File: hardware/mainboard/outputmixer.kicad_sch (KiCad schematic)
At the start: 15 parts, among them J1 EXT, J117 MIX, U12 TL074, U6 TL074

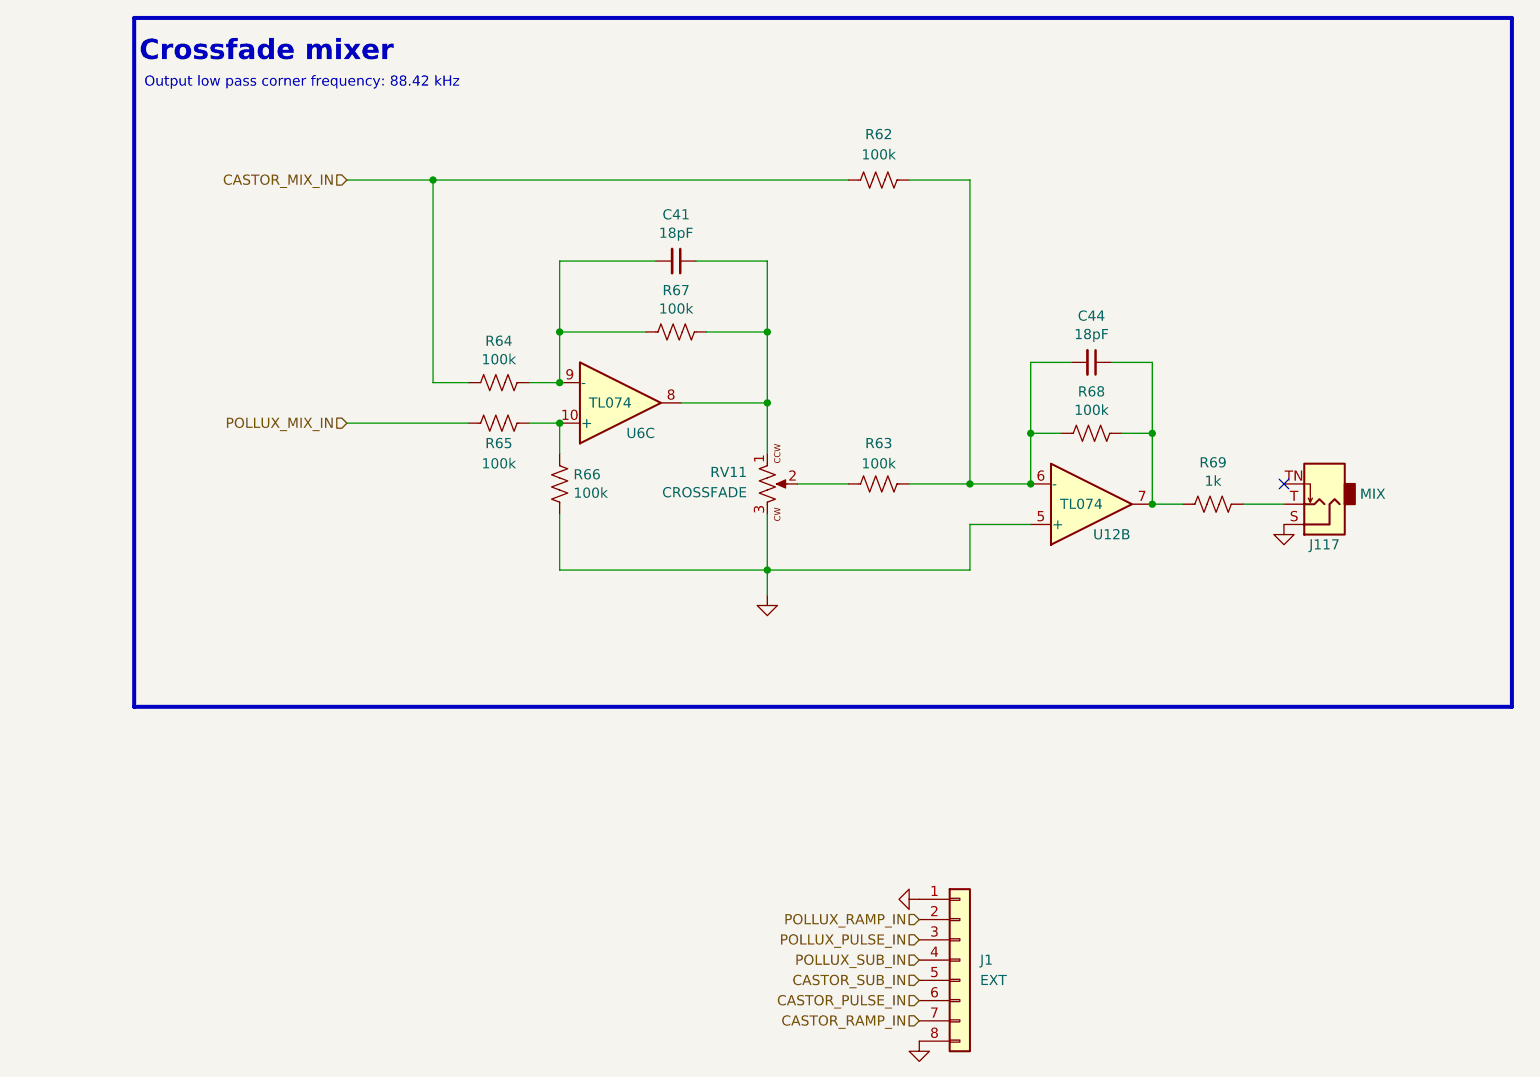
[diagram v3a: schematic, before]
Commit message: Reannotate schematic
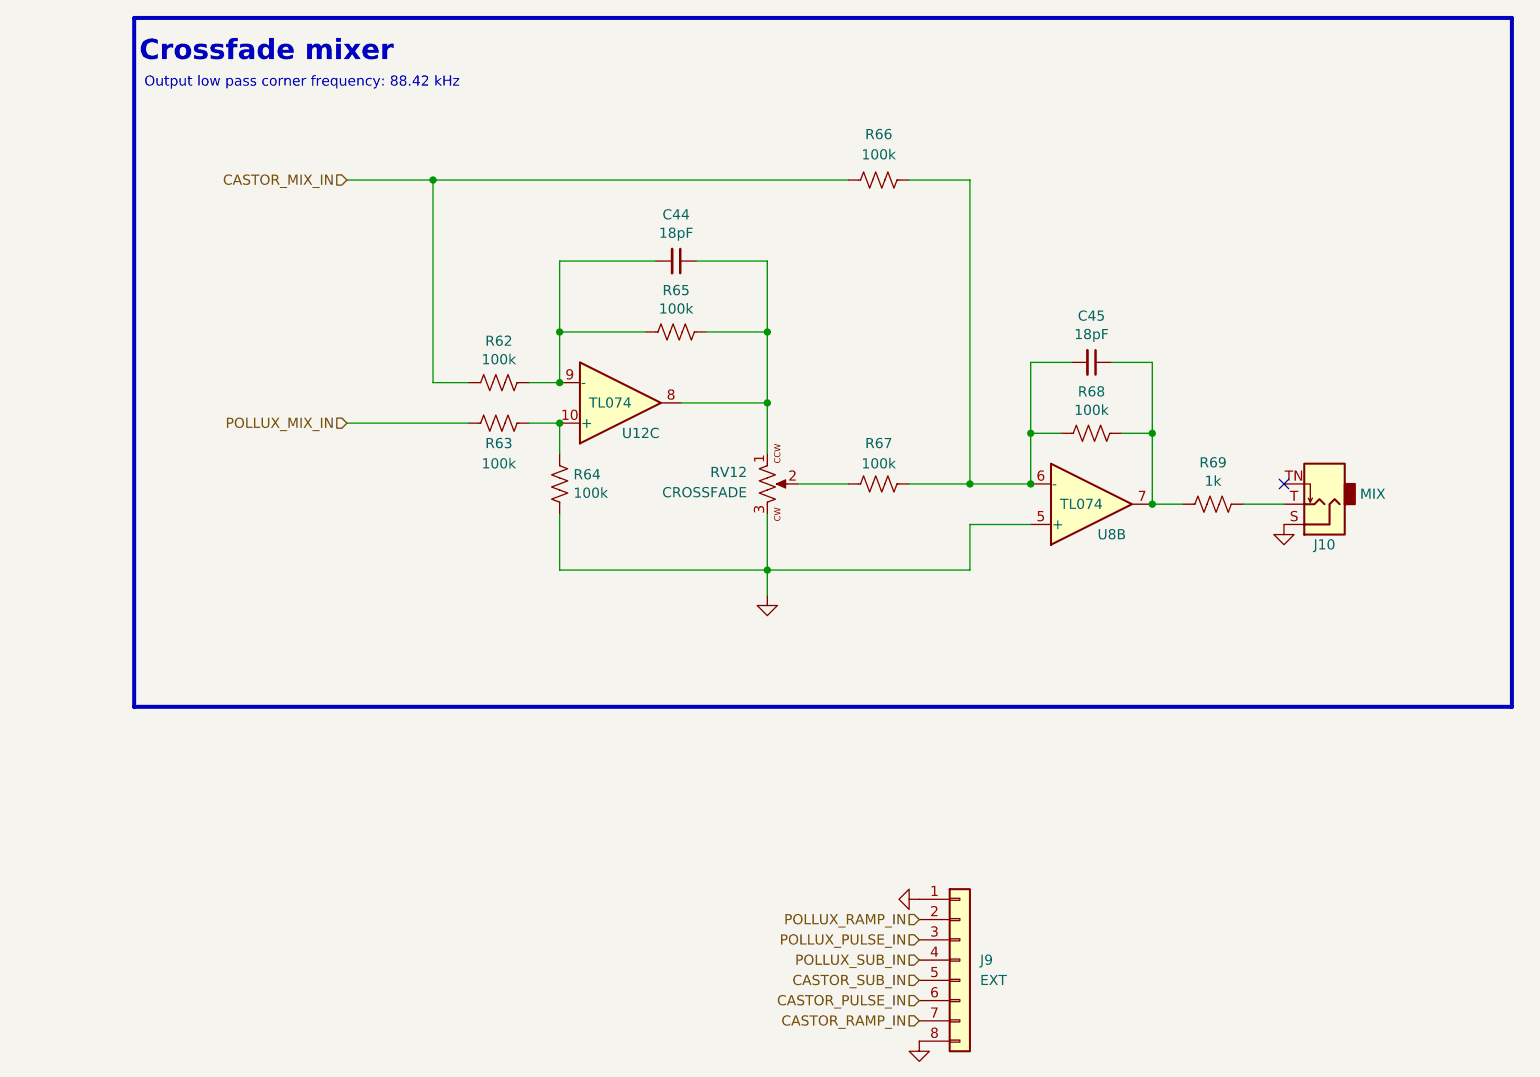
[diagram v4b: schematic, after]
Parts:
- renumbered C41 to C44, C44 to C45, J117 to J10, J1 to J9, R64 to R62, R65 to R63, R66 to R64, R67 to R65, R62 to R66, R63 to R67, RV11 to RV12, U6 to U12, U12 to U8
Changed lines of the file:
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@@
   (symbol (lib_id "Device:R_US") (at 99.695 69.85 270) (unit 1)
     (in_bom yes) (on_board yes)
-    (property "Reference" "R64" (id 0) (at 99.695 64.643 90))
+    (property "Reference" "R62" (id 0) (at 99.695 64.643 90))
     (property "Value" "100k" (id 1) (at 99.695 66.9544 90))
     (property "Footprint" "Resistor_SMD:R_0402_1005Metric_Pad0.72x0.64mm_HandSolder" (id 2) (at 99.441 70.866 90)
@@
   (symbol (lib_id "Device:R_US") (at 99.695 74.93 270) (unit 1)
     (in_bom yes) (on_board yes)
-    (property "Reference" "R65" (id 0) (at 99.695 77.47 90))
+    (property "Reference" "R63" (id 0) (at 99.695 77.47 90))
     (property "Value" "100k" (id 1) (at 99.695 80.01 90))
     (property "Footprint" "Resistor_SMD:R_0402_1005Metric_Pad0.72x0.64mm_HandSolder" (id 2) (at 99.441 75.946 90)
@@
   (symbol (lib_id "Device:R_US") (at 107.315 82.55 180) (unit 1)
     (in_bom yes) (on_board yes)
-    (property "Reference" "R66" (id 0) (at 109.0422 81.3816 0)
+    (property "Reference" "R64" (id 0) (at 109.0422 81.3816 0)
       (effects (font (size 1.27 1.27)) (justify right))
     )
@@
   (symbol (lib_id "Device:R_US") (at 121.92 63.5 90) (unit 1)
     (in_bom yes) (on_board yes)
-    (property "Reference" "R67" (id 0) (at 121.92 58.293 90))
+    (property "Reference" "R65" (id 0) (at 121.92 58.293 90))
     (property "Value" "100k" (id 1) (at 121.92 60.6044 90))
     (property "Footprint" "Resistor_SMD:R_0402_1005Metric_Pad0.72x0.64mm_HandSolder" (id 2) (at 122.174 62.484 90)
@@
   (symbol (lib_id "Device:R_US") (at 147.32 44.45 90) (unit 1)
     (in_bom yes) (on_board yes)
-    (property "Reference" "R62" (id 0) (at 147.32 38.735 90))
+    (property "Reference" "R66" (id 0) (at 147.32 38.735 90))
     (property "Value" "100k" (id 1) (at 147.32 41.275 90))
     (property "Footprint" "Resistor_SMD:R_0402_1005Metric_Pad0.72x0.64mm_HandSolder" (id 2) (at 147.574 43.434 90)
@@
   (symbol (lib_id "Device:C_Small") (at 121.92 54.61 270) (unit 1)
     (in_bom yes) (on_board yes)
-    (property "Reference" "C41" (id 0) (at 121.92 48.7934 90))
+    (property "Reference" "C44" (id 0) (at 121.92 48.7934 90))
     (property "Value" "18pF" (id 1) (at 121.92 51.1048 90))
     (property "Footprint" "Capacitor_SMD:C_0402_1005Metric_Pad0.74x0.62mm_HandSolder" (id 2) (at 121.92 54.61 0)
@@
   (symbol (lib_id "Device:R_US") (at 147.32 82.55 90) (unit 1)
     (in_bom yes) (on_board yes)
-    (property "Reference" "R63" (id 0) (at 147.32 77.47 90))
+    (property "Reference" "R67" (id 0) (at 147.32 77.47 90))
     (property "Value" "100k" (id 1) (at 147.32 80.01 90))
     (property "Footprint" "Resistor_SMD:R_0402_1005Metric_Pad0.72x0.64mm_HandSolder" (id 2) (at 147.574 81.534 90)
@@
   (symbol (lib_id "power:GND") (at 133.35 96.52 0) (unit 1)
     (in_bom yes) (on_board yes)
-    (property "Reference" "#PWR0120" (id 0) (at 133.35 102.87 0)
+    (property "Reference" "#PWR090" (id 0) (at 133.35 102.87 0)
       (effects (font (size 1.27 1.27)) hide)
     )
@@
   (symbol (lib_id "Device:C_Small") (at 173.99 67.31 270) (unit 1)
     (in_bom yes) (on_board yes)
-    (property "Reference" "C44" (id 0) (at 173.99 61.4934 90))
+    (property "Reference" "C45" (id 0) (at 173.99 61.4934 90))
     (property "Value" "18pF" (id 1) (at 173.99 63.8048 90))
     (property "Footprint" "Capacitor_SMD:C_0402_1005Metric_Pad0.74x0.62mm_HandSolder" (id 2) (at 173.99 67.31 0)
@@
   (symbol (lib_id "Connector_Generic:Conn_01x08") (at 157.48 142.24 0) (unit 1)
     (in_bom yes) (on_board yes) (fields_autoplaced)
-    (property "Reference" "J1" (id 0) (at 160.02 142.2399 0)
+    (property "Reference" "J9" (id 0) (at 160.02 142.2399 0)
       (effects (font (size 1.27 1.27)) (justify left))
     )
@@
   (symbol (lib_id "power:GND") (at 152.4 152.4 0) (unit 1)
     (in_bom yes) (on_board yes) (fields_autoplaced)
-    (property "Reference" "#PWR0128" (id 0) (at 152.4 158.75 0)
+    (property "Reference" "#PWR092" (id 0) (at 152.4 158.75 0)
       (effects (font (size 1.27 1.27)) hide)
     )
@@
   (symbol (lib_id "winterbloom:TL074") (at 173.99 85.09 0) (mirror x) (unit 2)
     (in_bom yes) (on_board yes)
-    (property "Reference" "U12" (id 0) (at 176.53 88.9 0))
+    (property "Reference" "U8" (id 0) (at 176.53 88.9 0))
     (property "Value" "TL074" (id 1) (at 172.72 85.09 0))
     (property "Footprint" "Package_SO:TSSOP-14_4.4x5mm_P0.65mm" (id 2) (at 173.99 95.25 0)
@@
   (symbol (lib_id "winterbloom:Eurorack_Mono_Jack") (at 203.2 83.82 0) (unit 1)
     (in_bom yes) (on_board yes)
-    (property "Reference" "J117" (id 0) (at 203.2 90.17 0))
+    (property "Reference" "J10" (id 0) (at 203.2 90.17 0))
     (property "Value" "MIX" (id 1) (at 207.645 83.82 0)
       (effects (font (size 1.27 1.27)) (justify left))
@@
   (symbol (lib_id "winterbloom:Eurorack_Pot") (at 133.35 82.55 90) (mirror x) (unit 1)
     (in_bom yes) (on_board yes) (fields_autoplaced)
-    (property "Reference" "RV11" (id 0) (at 130.81 81.0894 90)
+    (property "Reference" "RV12" (id 0) (at 130.81 81.0894 90)
       (effects (font (size 1.27 1.27)) (justify left))
     )
@@
   (symbol (lib_id "winterbloom:TL074") (at 114.935 72.39 0) (mirror x) (unit 3)
     (in_bom yes) (on_board yes)
-    (property "Reference" "U6" (id 0) (at 117.475 76.2 0))
+    (property "Reference" "U12" (id 0) (at 117.475 76.2 0))
     (property "Value" "TL074" (id 1) (at 113.665 72.39 0))
     (property "Footprint" "Package_SO:TSSOP-14_4.4x5mm_P0.65mm" (id 2) (at 114.935 82.55 0)
@@
   (symbol (lib_id "power:GND") (at 152.4 134.62 270) (unit 1)
     (in_bom yes) (on_board yes) (fields_autoplaced)
-    (property "Reference" "#PWR0129" (id 0) (at 146.05 134.62 0)
+    (property "Reference" "#PWR091" (id 0) (at 146.05 134.62 0)
       (effects (font (size 1.27 1.27)) hide)
     )
@@
   (symbol (lib_id "power:GND") (at 198.12 87.63 0) (unit 1)
     (in_bom yes) (on_board yes)
-    (property "Reference" "#PWR0155" (id 0) (at 198.12 93.98 0)
-      (effects (font (size 1.27 1.27)) hide)
-    )
+    (property "Reference" "#PWR093" (id 0) (at 198.12 93.98 0)
+      (effects (font (size 1.27 1.27)) hide)
+    )

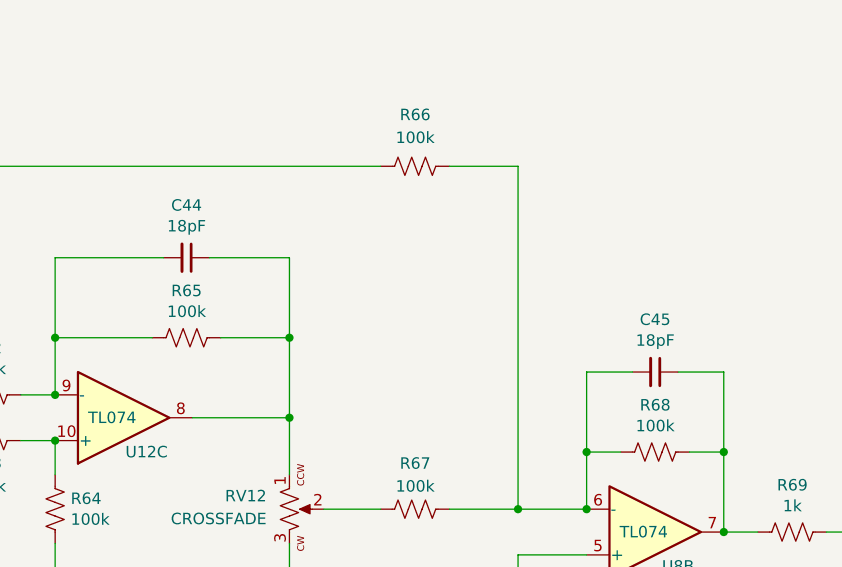
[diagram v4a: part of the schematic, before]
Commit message: Normalize component values
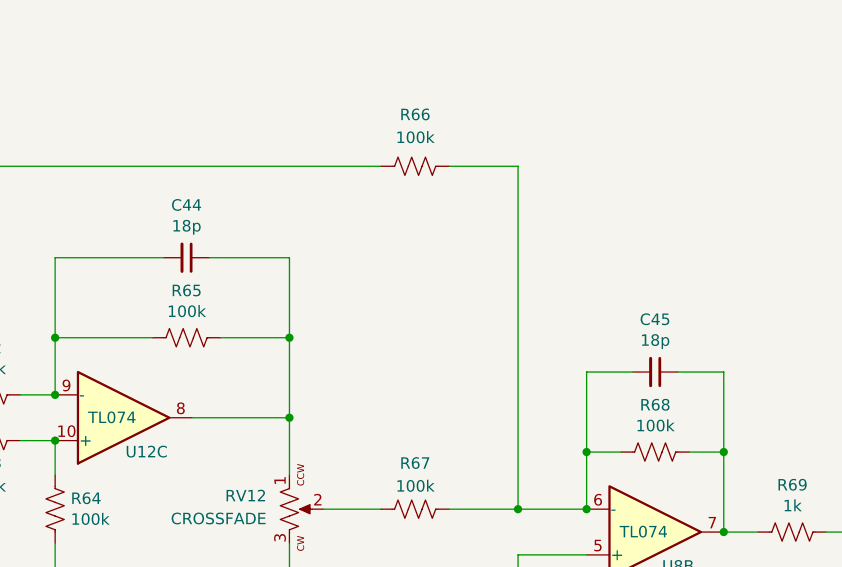
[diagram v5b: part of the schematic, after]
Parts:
- C44, C45: value 18pF -> 18p
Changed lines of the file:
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@@
     (in_bom yes) (on_board yes)
     (property "Reference" "C44" (id 0) (at 121.92 48.7934 90))
-    (property "Value" "18pF" (id 1) (at 121.92 51.1048 90))
+    (property "Value" "18p" (id 1) (at 121.92 51.1048 90))
     (property "Footprint" "Capacitor_SMD:C_0402_1005Metric_Pad0.74x0.62mm_HandSolder" (id 2) (at 121.92 54.61 0)
       (effects (font (size 1.27 1.27)) hide)
@@
     (in_bom yes) (on_board yes)
     (property "Reference" "C45" (id 0) (at 173.99 61.4934 90))
-    (property "Value" "18pF" (id 1) (at 173.99 63.8048 90))
+    (property "Value" "18p" (id 1) (at 173.99 63.8048 90))
     (property "Footprint" "Capacitor_SMD:C_0402_1005Metric_Pad0.74x0.62mm_HandSolder" (id 2) (at 173.99 67.31 0)
       (effects (font (size 1.27 1.27)) hide)

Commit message: Switch audio filter caps to 0603. Start auditing BOM
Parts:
- C44, C45: Reqs audio filter, 16v+ -> Eurorack level audio filter, 16 V; finalized yes -> (none); mpn MF-CAP-0603-18pF -> (none); mpn alt GCM1885C2A180JA16D -> (none); mpn specs 5% 50v -> (none)
- J10: finalized (none) -> yes
- R62, R63, R64, R65, R66, R67, R68: Reqs 1%, 2mW, audio path -> Eurorack level audio, 1%, 2 mW; finalized yes -> (none); mpn RR0816P-104-D -> (none); mpn alt ERA-3AED104V -> (none); mpn specs 62mW, 0.5% -> (none)
- R69: Reqs 5%, audio path -> Output impedance, 5%, 150 mW; finalized yes -> (none); mpn MCT06030C1001FP500 -> MCT06030C1001FP500, ERA-3AEB102V; mpn alt ERA-3AEB102V -> (none); mpn specs 100mW, 1% -> (none)
